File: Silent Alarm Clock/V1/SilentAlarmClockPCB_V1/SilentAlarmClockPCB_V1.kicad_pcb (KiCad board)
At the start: 2 copper layers, 28 parts, among them J1 USB_C_Receptacle_USB2.0_16P, J2 Barrel_Jack, J3 B2B-PH-K-S, SW1 BOOT, SW2 RESET, U2 ESP32-S3-MINI-1-N8, U3 BQ24040DSQR, U4 TLV75801PDRV, U5 ESD7104MUTAG

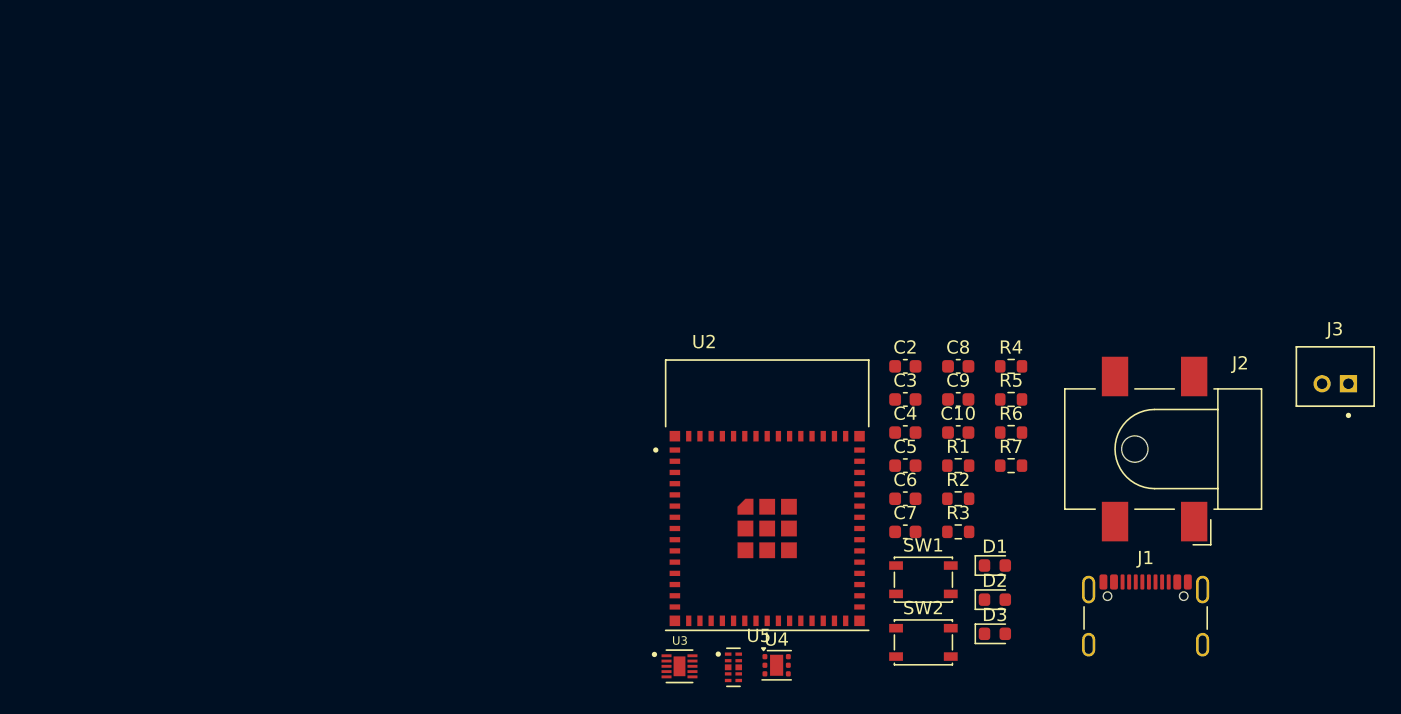
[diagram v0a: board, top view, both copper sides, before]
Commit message: fixed push button switch footprints
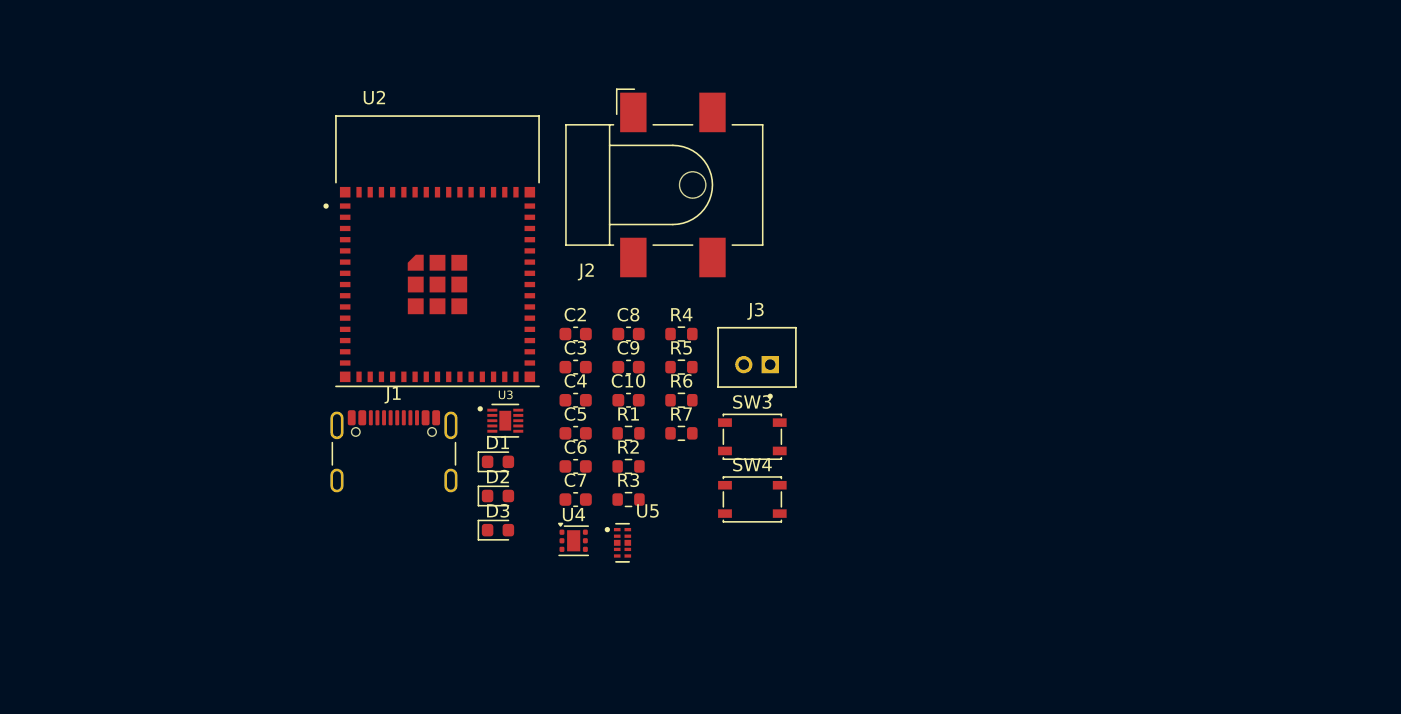
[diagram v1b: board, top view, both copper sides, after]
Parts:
- removed SW1: BOOT, Button_Switch_SMD:SW_SPST_PTS810
- removed SW2: RESET, Button_Switch_SMD:SW_SPST_PTS810
- added SW3: RESET, Button_Switch_SMD:SW_SPST_PTS810, F.Cu at (81.5, 60.1)
- added SW4: BOOT, Button_Switch_SMD:SW_SPST_PTS810, F.Cu at (81.5, 64.8)
- moved J1 58.3 mm to (54.3, 62.3)
- moved J3 43.9 mm to (81.9, 54.1)
- moved J2 41.7 mm to (75.5, 41.0), turned to 0 degrees
- moved D1 38.5 mm to (62.2, 62.0)
- moved D2 38.5 mm to (62.2, 64.6)
- moved D3 38.5 mm to (62.2, 67.2)
- moved U2 31.1 mm to (57.6, 48.5)
- moved C10 25.1 mm to (72.1, 57.3)
- moved C2 25.1 mm to (68.1, 52.3)
- moved C3 25.1 mm to (68.1, 54.8)
- moved C4 25.1 mm to (68.1, 57.3)
- moved C5 25.1 mm to (68.1, 59.8)
- moved C6 25.1 mm to (68.1, 62.3)
- moved C7 25.1 mm to (68.1, 64.9)
- moved C8 25.1 mm to (72.1, 52.3)
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
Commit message: Finished V1 board
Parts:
- removed U5: ESD7104MUTAG, ESD7104MUTAG:IC_ESD7104MUTAG
- added U1: ESD7104MUTAG, ESD7104MUTAG:UDFN10_ONS, F.Cu at (39.4, 55.0)
- moved J2 40.7 mm to (35.0, 37.0)
- moved J3 39.6 mm to (49.0, 31.9)
- moved C6 38.6 mm to (44.0, 32.3), turned to -90 degrees
- moved R2 33.5 mm to (42.5, 46.7), turned to -90 degrees
- moved R3 33.1 mm to (42.5, 50.0), turned to -90 degrees
- moved SW4 32.8 mm to (68.9, 34.6)
- moved C7 30.8 mm to (75.7, 35.0)
- moved R4 29.8 mm to (48.0, 42.6)
- moved U4 28.7 mm to (46.5, 49.0)
- moved C2 27.5 mm to (45.0, 37.4), turned to -90 degrees
- moved J1 26.6 mm to (29.1, 54.2), turned to -90 degrees
- moved C5 25.6 mm to (46.3, 46.5)
- moved R5 25.2 mm to (54.5, 42.0), turned to -90 degrees
- moved U3 24.4 mm to (48.0, 39.5)
- moved R6 24.1 mm to (57.5, 42.0), turned to -90 degrees
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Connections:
- C7 pad 1: Net-(U2-3V3) -> /3V3
- C8 pad 1: Net-(U2-3V3) -> /3V3
- R1 pad 1: Net-(U2-3V3) -> /3V3
- U2 pad 3: Net-(U2-3V3) -> /3V3
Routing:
- net /3V3: track 0.00 -> 78.3 mm, vias 0 -> 2
- net GND: track 0.00 -> 58.2 mm, vias 0 -> 68
- net Net-(U3-OUT): track 0.00 -> 41.5 mm
- net /5VIN: track 0.00 -> 40.1 mm, vias 0 -> 10
- net /USB_N: track 0.00 -> 37.1 mm
- net /USB_P: track 0.00 -> 36.7 mm
- net Net-(U2-EN): track 0.00 -> 18.8 mm
- net Net-(D2-K): track 0.00 -> 12.1 mm
- net Net-(U2-IO0): track 0.00 -> 11.1 mm
- net Net-(D1-K): track 0.00 -> 9.88 mm
- net Net-(J1-VBUS-PadA4): track 0.00 -> 6.21 mm
- net Net-(U4-FB): track 0.00 -> 4.86 mm
- net Net-(U3-ISET): track 0.00 -> 4.54 mm
- net Net-(D3-A): track 0.00 -> 1.67 mm
- net Net-(D2-A): track 0.00 -> 1.67 mm
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- added copper zone on In2.Cu, net /5VIN
- added copper zone on B.Cu, net GND
- added copper zone on F.Cu, net GND
- added copper zone on In1.Cu, net GND
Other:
- board outline added: 52 x 31 mm
- copper layers 2 -> 4
